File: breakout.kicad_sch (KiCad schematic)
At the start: 1 part, among them J1 Conn_02x05_Odd_Even

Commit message: tps568230
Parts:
- added C1: 1uF, symbol Device:C
- added C2, C4: 1uF, symbol Device:C_Small
- added C3: 100uF, symbol Device:C_Small
- added F1, F2, F3, F4: Polyfuse, symbol Device:Polyfuse
- added J10, J7, J8, J9: SATA_Power_15P_Male, SATA_Power_Male:SATA_Power_15P_Male_Angled_THT, symbol SATA_Power_Male:SATA_Power_15P_Male
- added L1: 2.2uH, symbol Device:L
- added R1: 33kR, symbol Device:R_US
- added R2: 100kR, symbol Device:R_US
- added R3: 330kR, symbol Device:R_US
- added R4: 5.1kR, symbol Device:R_US
- added R5: 30kR, symbol Device:R_Small_US
- added R6: 220kR, symbol Device:R_Small_US
- added U1: TPS568230, Package_DFN_QFN:Texas_RJE0020A_VQFN-20-1EP_3x3mm_P0.45mm_EP0.675x0.76mm, symbol Regulator_Switching:TPS568230
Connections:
- net +5VSB is gone; now on net GND: J1.10 (Pin_10)
- net PS_ON is gone; now on net +12V: J1.9 (Pin_9)
- net +12V: now also J1.7 (Pin_7), F2.2, F4.1; no longer J1.1 (Pin_1), J1.2 (Pin_2), J1.3 (Pin_3), J1.4 (Pin_4)
- net GND: now also J1.3 (Pin_3), J1.4 (Pin_4), C1.1, C2.1, C3.1, J10.10 (GND), J10.11 (GND), J10.12 (GND), J10.4 (GND), J10.5 (GND), J10.6 (GND), J7.10 (GND), J7.11 (GND), J7.12 (GND), J7.4 (GND), J7.5 (GND), J7.6 (GND), J8.10 (GND), J8.11 (GND), J8.12 (GND), J8.4 (GND), J8.5 (GND), J8.6 (GND), J9.10 (GND), J9.11 (GND), J9.12 (GND), J9.4 (GND), J9.5 (GND), J9.6 (GND), R1.2, R4.1, R5.2, U1.13 (AGND), U1.18 (GND), U1.21 (GND), U1.7 (GND), U1.8 (GND); no longer J1.5 (Pin_5), J1.6 (Pin_6), J1.7 (Pin_7)
- new net: C1.2, F2.1, R2.1, U1.2 (VIN), U1.3 (VIN), U1.4 (VIN), U1.5 (VIN)
- new net: R1.1, R2.2, U1.12 (EN)
- new net: C4.2, U1.1 (BST)
- new net: U1.10 (NC), U1.16 (NC)
- new net: R5.1, R6.2, U1.14 (FB)
- new net: R3.2, R4.2, U1.15 (MODE)
- new net: C2.2, R3.1, U1.17 (VCC)
- new net: C4.1, L1.1, U1.19 (SW), U1.20 (SW), U1.6 (SW)
- new net +3V3: F1.1, J1.1 (Pin_1)
- new net +5V: C3.2, F3.1, L1.2, R6.1
- new net 12V_SATA1: F4.2, J10.13 (+12V), J10.14 (+12V), J10.15 (+12V), J7.13 (+12V), J7.14 (+12V), J7.15 (+12V), J8.13 (+12V), J8.14 (+12V), J8.15 (+12V), J9.13 (+12V), J9.14 (+12V), J9.15 (+12V)
- new net 3V3: J1.2 (Pin_2)
- new net 3V3_SATA1: F1.2, J10.1 (+3V3), J10.2 (+3V3), J10.3 (+3V3/PWDIS), J7.1 (+3V3), J7.2 (+3V3), J7.3 (+3V3/PWDIS), J8.1 (+3V3), J8.2 (+3V3), J8.3 (+3V3/PWDIS), J9.1 (+3V3), J9.2 (+3V3), J9.3 (+3V3/PWDIS)
- new net 5VSB: J1.5 (Pin_5)
- new net 5V_SATA1: F3.2, J10.7 (+5V), J10.8 (+5V), J10.9 (+5V), J7.7 (+5V), J7.8 (+5V), J7.9 (+5V), J8.7 (+5V), J8.8 (+5V), J8.9 (+5V), J9.7 (+5V), J9.8 (+5V), J9.9 (+5V)
- new net PWOn: J1.6 (Pin_6)
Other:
- moved on the sheet: J1

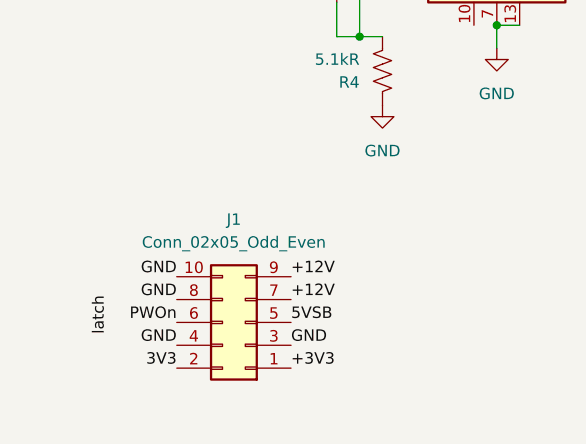
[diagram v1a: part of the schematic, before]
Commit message: add button to short PSON to GND
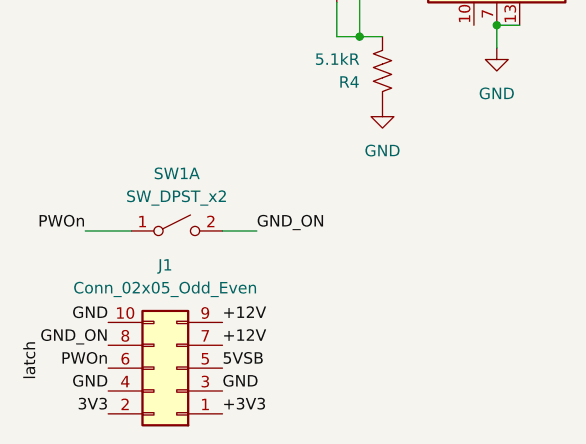
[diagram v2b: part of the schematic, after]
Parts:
- added SW1: SW_DPST_x2, symbol Switch:SW_DPST_x2
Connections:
- net GND: no longer J1.8 (Pin_8)
- net PWOn: now also SW1.1 (A)
- new net GND_ON: J1.8 (Pin_8), SW1.2 (B)
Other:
- moved on the sheet: J1
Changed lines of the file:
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@@
 	)
 	(junction
-		(at 39.37 86.36)
+		(at 165.1 134.62)
 		(diameter 0)
 		(color 0 0 0 0)
 	)
 	(junction
-		(at 80.01 38.1)
+		(at 39.37 86.36)
 		(diameter 0)
 		(color 0 0 0 0)
 	)
 	(junction
-		(at 165.1 134.62)
+		(at 80.01 38.1)
 		(diameter 0)
 		(color 0 0 0 0)
@@
 	(wire
 		(pts
+			(xy 35.56 137.16) (xy 40.64 137.16)
+		)
+		(stroke
+			(width 0)
+			(type default)
+		)
+	)
+	(wire
+		(pts
 			(xy 165.1 76.2) (xy 176.53 76.2)
 		)
@@
 	(wire
 		(pts
+			(xy 50.8 137.16) (xy 54.61 137.16)
+		)
+		(stroke
+			(width 0)
+			(type default)
+		)
+	)
+	(wire
+		(pts
 			(xy 223.52 38.1) (xy 226.06 38.1)
 		)
@@
 		)
 	)
+	(label "GND_ON"
+		(at 54.61 137.16 0)
+		(effects
+			(font
+				(size 1.27 1.27)
+			)
+			(justify left bottom)
+		)
+	)
 	(label "12V_SATA3"
 		(at 177.8 132.08 0)
@@
 	)
 	(label "GND"
-		(at 58.42 149.86 0)
+		(at 50.8 154.94 0)
 		(effects
 			(font
@@
 	)
 	(label "5VSB"
-		(at 58.42 147.32 0)
+		(at 50.8 152.4 0)
 		(effects
 			(font
@@
 	)
 	(label "PWOn"
-		(at 45.72 147.32 180)
+		(at 38.1 152.4 180)
 		(effects
 			(font
@@
 	)
 	(label "GND"
-		(at 45.72 149.86 180)
+		(at 38.1 154.94 180)
 		(effects
 			(font
@@
 		)
 	)
-	(label "GND"
-		(at 45.72 144.78 180)
+	(label "GND_ON"
+		(at 38.1 149.86 180)
 		(effects
 			(font
@@
 	)
 	(label "+12V"
-		(at 58.42 142.24 0)
+		(at 50.8 147.32 0)
 		(effects
 			(font
@@
 	)
 	(label "3V3"
-		(at 45.72 152.4 180)
+		(at 38.1 157.48 180)
 		(effects
 			(font
@@
 	)
 	(label "+12V"
-		(at 58.42 144.78 0)
+		(at 50.8 149.86 0)
 		(effects
 			(font
@@
 		)
 	)
+	(label "PWOn"
+		(at 35.56 137.16 180)
+		(effects
+			(font
+				(size 1.27 1.27)
+			)
+			(justify right bottom)
+		)
+	)
 	(label "5V_SATA4"
 		(at 177.8 107.95 0)
@@
 	)
 	(label "GND"
-		(at 45.72 142.24 180)
+		(at 38.1 147.32 180)
 		(effects
 			(font
@@
 	)
 	(label "latch"
-		(at 38.1 148.59 90)
+		(at 30.48 153.67 90)
 		(effects
 			(font
@@
 	)
 	(label "+3V3"
-		(at 58.42 152.4 0)
+		(at 50.8 157.48 0)
 		(effects
 			(font
@@
 	)
 	(symbol
+		(lib_id "Switch:SW_DPST_x2")
+		(at 45.72 137.16 0)
+		(unit 1)
+		(body_style 1)
+		(exclude_from_sim no)
+		(in_bom yes)
+		(on_board yes)
+		(in_pos_files yes)
+		(dnp no)
+		(fields_autoplaced yes)
+		(property "Reference" "SW1"
+			(at 45.72 130.81 0)
+			(show_name no)
+			(do_not_autoplace no)
+			(effects
+				(font
+					(size 1.27 1.27)
+				)
+			)
+		)
+		(property "Value" "SW_DPST_x2"
+			(at 45.72 133.35 0)
+			(show_name no)
+			(do_not_autoplace no)
+			(effects
+				(font
+					(size 1.27 1.27)
+				)
+			)
+		)
+		(property "Footprint" ""
+			(at 45.72 137.16 0)
+			(hide yes)
+			(show_name no)
+			(do_not_autoplace no)
+			(effects
+				(font
+					(size 1.27 1.27)
+				)
+			)
+		)
+		(property "Datasheet" ""
+			(at 45.72 137.16 0)
+			(hide yes)
+			(show_name no)
+			(do_not_autoplace no)
+			(effects
+				(font
+					(size 1.27 1.27)
+				)
+			)
+		)
+		(property "Description" "Single Pole Single Throw (SPST) switch, separate symbol"
+			(at 45.72 137.16 0)
+			(hide yes)
+			(show_name no)
+			(do_not_autoplace no)
+			(effects
+				(font
+					(size 1.27 1.27)
+				)
+			)
+		)
+		(pin "4"
+		)
+		(pin "1"
+		)
+		(pin "2"
+		)
+		(pin "3"
+		)
+		(instances
+			(project "breakout"
+				(path "/e7acdc49-5583-42b4-8c0e-d4aaccb46e47"
+					(reference "SW1")
+					(unit 1)
+				)
+			)
+		)
+	)
+	(symbol
 		(lib_id "power:GND")
 		(at 110.49 76.2 180)
@@
 	(symbol
 		(lib_id "Connector_Generic:Conn_02x05_Odd_Even")
-		(at 53.34 147.32 180)
+		(at 45.72 152.4 180)
 		(unit 1)
 		(body_style 1)
@@
 		(dnp no)
 		(property "Reference" "J1"
-			(at 52.07 135.89 0)
+			(at 44.45 140.97 0)
 			(show_name no)
 			(do_not_autoplace no)
@@
 		)
 		(property "Value" "Conn_02x05_Odd_Even"
-			(at 52.07 138.43 0)
+			(at 44.45 143.51 0)
 			(show_name no)
 			(do_not_autoplace no)
@@
 		)
 		(property "Footprint" ""
-			(at 53.34 147.32 0)
+			(at 45.72 152.4 0)
 			(hide yes)
 			(show_name no)
@@
 		)
 		(property "Datasheet" ""
-			(at 53.34 147.32 0)
+			(at 45.72 152.4 0)
 			(hide yes)
 			(show_name no)
@@
 		)
 		(property "Description" "Generic connector, double row, 02x05, odd/even pin numbering scheme (row 1 odd numbers, row 2 even numbers), script generated (kicad-library-utils/schlib/autogen/connector/)"
-			(at 53.34 147.32 0)
+			(at 45.72 152.4 0)
 			(hide yes)
 			(show_name no)

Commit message: updt
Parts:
- added J2: USB_C_Receptacle_USB2.0_16P, symbol Connector:USB_C_Receptacle_USB2.0_16P
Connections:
- new net: J2.A1 (GND), J2.A12 (GND), J2.B1 (GND), J2.B12 (GND)
- new net: J2.A4 (VBUS), J2.A9 (VBUS), J2.B4 (VBUS), J2.B9 (VBUS)
- no-connect marks 0 -> 2
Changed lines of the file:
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@@
 		(color 0 0 0 0)
 	)
+	(no_connect
+		(at 66.04 231.14)
+	)
+	(no_connect
+		(at 66.04 228.6)
+	)
 	(wire
 		(pts
@@
 					(unit 1)
 				)
+			)
+		)
+	)
+	(symbol
+		(lib_id "Connector:USB_C_Receptacle_USB2.0_16P")
+		(at 50.8 215.9 0)
+		(unit 1)
+		(body_style 1)
+		(exclude_from_sim no)
+		(in_bom yes)
+		(on_board yes)
+		(in_pos_files yes)
+		(dnp no)
+		(fields_autoplaced yes)
+		(property "Reference" "J2"
+			(at 50.8 193.04 0)
+			(show_name no)
+			(do_not_autoplace no)
+			(effects
+				(font
+					(size 1.27 1.27)
+				)
+			)
+		)
+		(property "Value" "USB_C_Receptacle_USB2.0_16P"
+			(at 50.8 195.58 0)
+			(show_name no)
+			(do_not_autoplace no)
+			(effects
+				(font
+					(size 1.27 1.27)
+				)
+			)
+		)
+		(property "Footprint" ""
+			(at 54.61 215.9 0)
+			(hide yes)
+			(show_name no)
+			(do_not_autoplace no)
+			(effects
+				(font
+					(size 1.27 1.27)
+				)
+			)
+		)
+		(property "Datasheet" "https://www.usb.org/sites/default/files/documents/usb_type-c.zip"
+			(at 54.61 215.9 0)
+			(hide yes)
+			(show_name no)
+			(do_not_autoplace no)
+			(effects
+				(font
+					(size 1.27 1.27)
+				)
+			)
+		)
+		(property "Description" "USB 2.0-only 16P Type-C Receptacle connector"
+			(at 50.8 215.9 0)
+			(hide yes)
+			(show_name no)
+			(do_not_autoplace no)
+			(effects
+				(font
+					(size 1.27 1.27)
+				)
+			)
+		)
+		(pin "B7"
+		)
+		(pin "B9"
+		)
+		(pin "B1"
+		)
+		(pin "B5"
+		)
+		(pin "A12"
+		)
+		(pin "B12"
+		)
+		(pin "B4"
+		)
+		(pin "B6"
+		)
+		(pin "SH"
+		)
+		(pin "A1"
+		)
+		(pin "B8"
+		)
+		(pin "A4"
+		)
+		(pin "A6"
+		)
+		(pin "A9"
+		)
+		(pin "A8"
+		)
+		(pin "A5"
+		)
+		(pin "A7"
+		)
+		(instances
+			(project "breakout"
+				(path "/e7acdc49-5583-42b4-8c0e-d4aaccb46e47"
+					(reference "J2")
+					(unit 1)
+				)

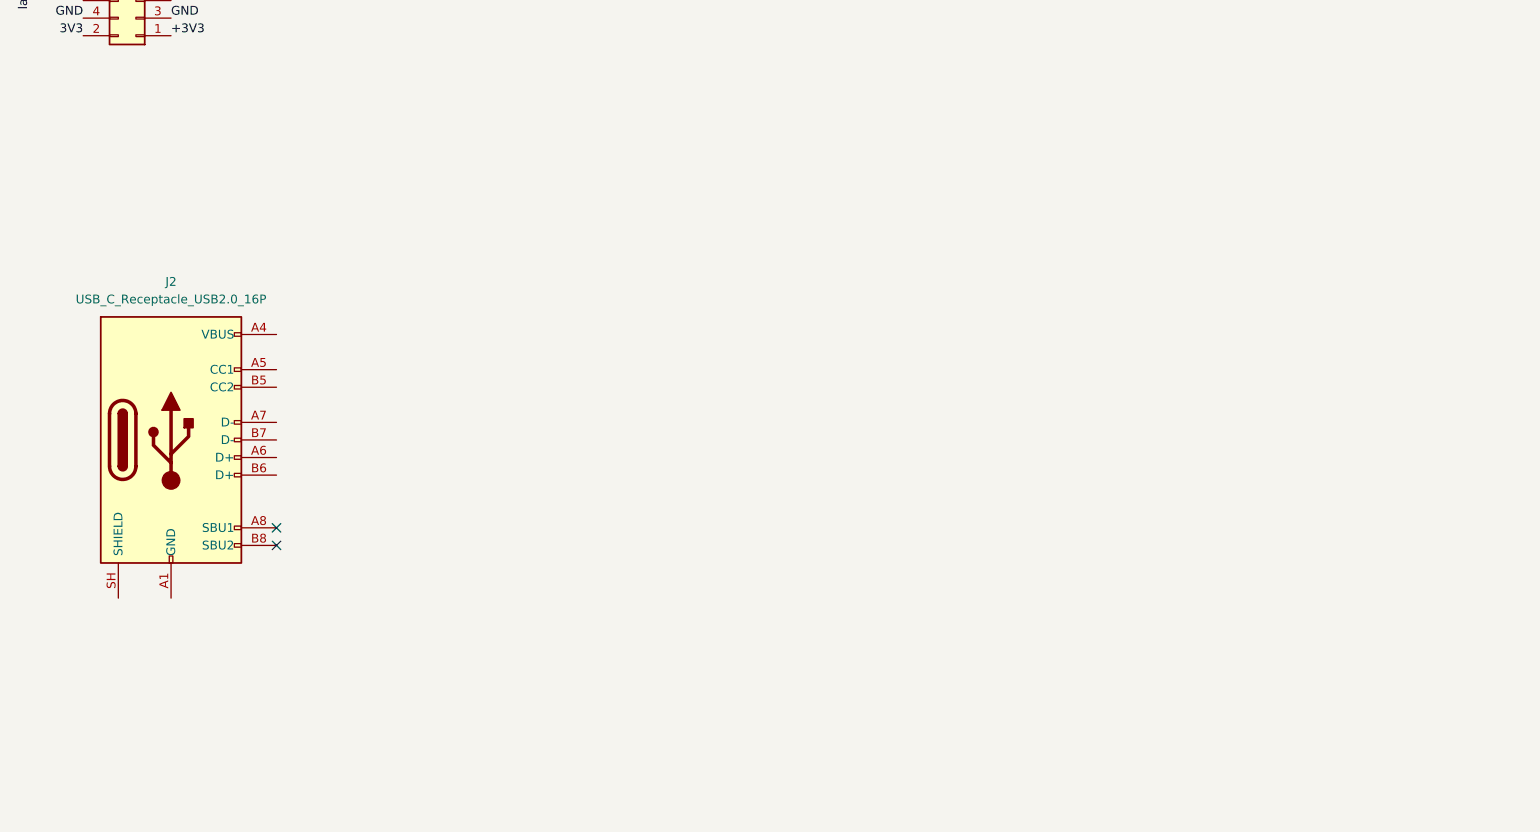
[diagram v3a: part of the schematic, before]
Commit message: fix sata footprint
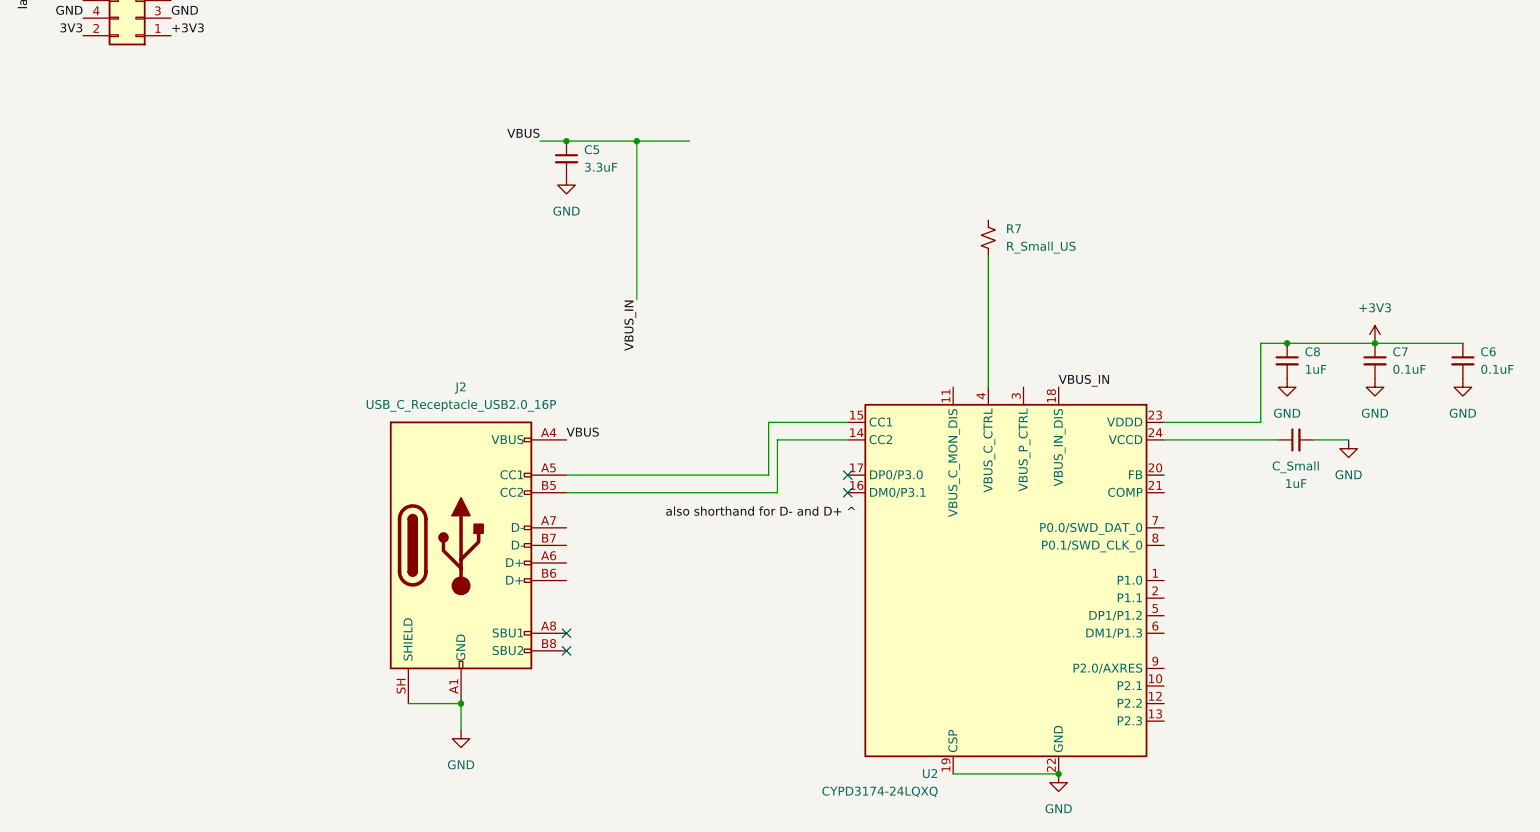
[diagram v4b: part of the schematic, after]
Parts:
- added 1uF: C_Small, symbol Device:C_Small
- added C5: 3.3uF, symbol Device:C_Small
- added C6, C7: 0.1uF, symbol Device:C_Small
- added C8: 1uF, symbol Device:C_Small
- added R7: R_Small_US, symbol Device:R_Small_US
- added U2: CYPD3174-24LQXQ, Package_DFN_QFN:QFN-24-1EP_4x4mm_P0.5mm_EP2.75x2.75mm, symbol Interface_USB:CYPD3174-24LQXQ
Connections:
- net +3V3: now also C6.1, C7.1, C8.1, U2.23 (VDDD)
- net GND: now also J2.A1 (GND), J2.A12 (GND), J2.B1 (GND), J2.B12 (GND), J2.SH (SHIELD), 1uF.2, C5.2, C6.2, C7.2, C8.2, U2.19 (CSP), U2.22 (GND), U2.25 (GND)
- net VBUS: now reaches J2.A4 (VBUS), J2.A9 (VBUS), J2.B4 (VBUS), J2.B9 (VBUS)
- net VBUS: now also C5.1, U2.18 (VBUS_IN_DIS)
- net at J2.A5 (CC1): now also U2.15 (CC1)
- net at J2.B5 (CC2): now also U2.14 (CC2)
- new net: 1uF.1, U2.24 (VCCD)
- new net: R7.2, U2.4 (VBUS_C_CTRL)
- no-connect marks 2 -> 4
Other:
- moved on the sheet: J2

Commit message: feat :implement cypd3174??
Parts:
- removed R7: R_Small_US, symbol Device:R_Small_US
- added C11, C9: 1uF, symbol Device:C_Small
- added D1: 15V, Diode_THT:D_DO-41_SOD81_P10.16mm_Horizontal, symbol Diode:1N4003
- added D2: LED_Small, symbol Device:LED_Small
- added Q1, Q2: DMP3013SFV, Package_SON:Diodes_PowerDI3333-8, symbol Transistor_FET:DMP3013SFV
- added R10, R13, R14: 5.1kR, symbol Device:R_Small_US
- added R11, R12, R15: 2.4kR, symbol Device:R_Small_US
- added R8: 10kR, symbol Device:R_Small_US
- added R9: 49.9kR, symbol Device:R_Small_US
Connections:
- net +12V: now also C11.1, Q2.1 (S), Q2.2 (S), Q2.3 (S)
- net +3V3: now also R10.1, R13.1
- net GND: now also U2.1 (P1.0), U2.6 (DM1/P1.3), C11.2, D2.1 (K), R11.2, R12.2
- net at U2.2 (P1.1): now also R10.2, R11.1
- net at U2.3 (VBUS_P_CTRL): now also R15.2
- net at U2.5 (DP1/P1.2): now also R12.1, R13.2
- net at U2.9 (P2.0/AXRES): now also R14.2
- net VBUS renamed VBUS_IN
- net VBUS_IN: now also C9.1, Q1.5 (D), R8.1
- new net: D2.2 (A), R14.1
- new net: C9.2, D1.2 (A), Q1.4 (G), Q2.4 (G), R15.1, R8.2, R9.2
- new net: D1.1 (K), Q1.1 (S), Q1.2 (S), Q1.3 (S), Q2.5 (D), R9.1
- no-connect marks 4 -> 13
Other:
- moved on the sheet: 1uF, C5, C6, C7, C8, J2, U2
